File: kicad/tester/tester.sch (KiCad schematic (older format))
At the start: 9 parts, among them J0 ST7735, U1 STM32F103C8Tx, U2 LMV324, Y1 8Mhz

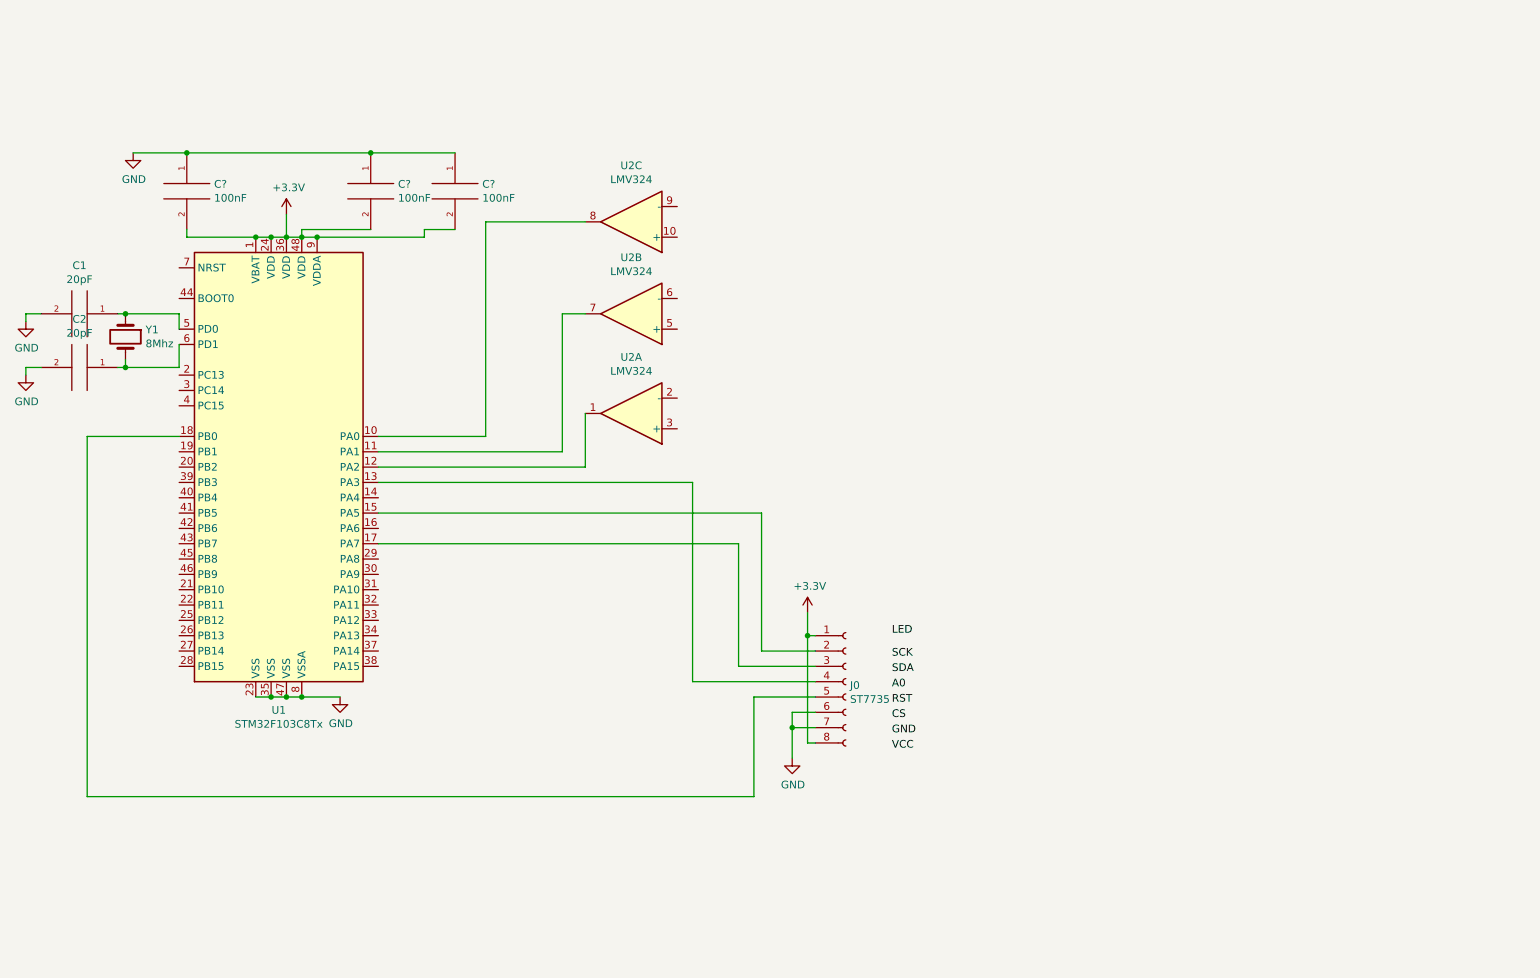
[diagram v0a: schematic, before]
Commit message: kicad : update schematic
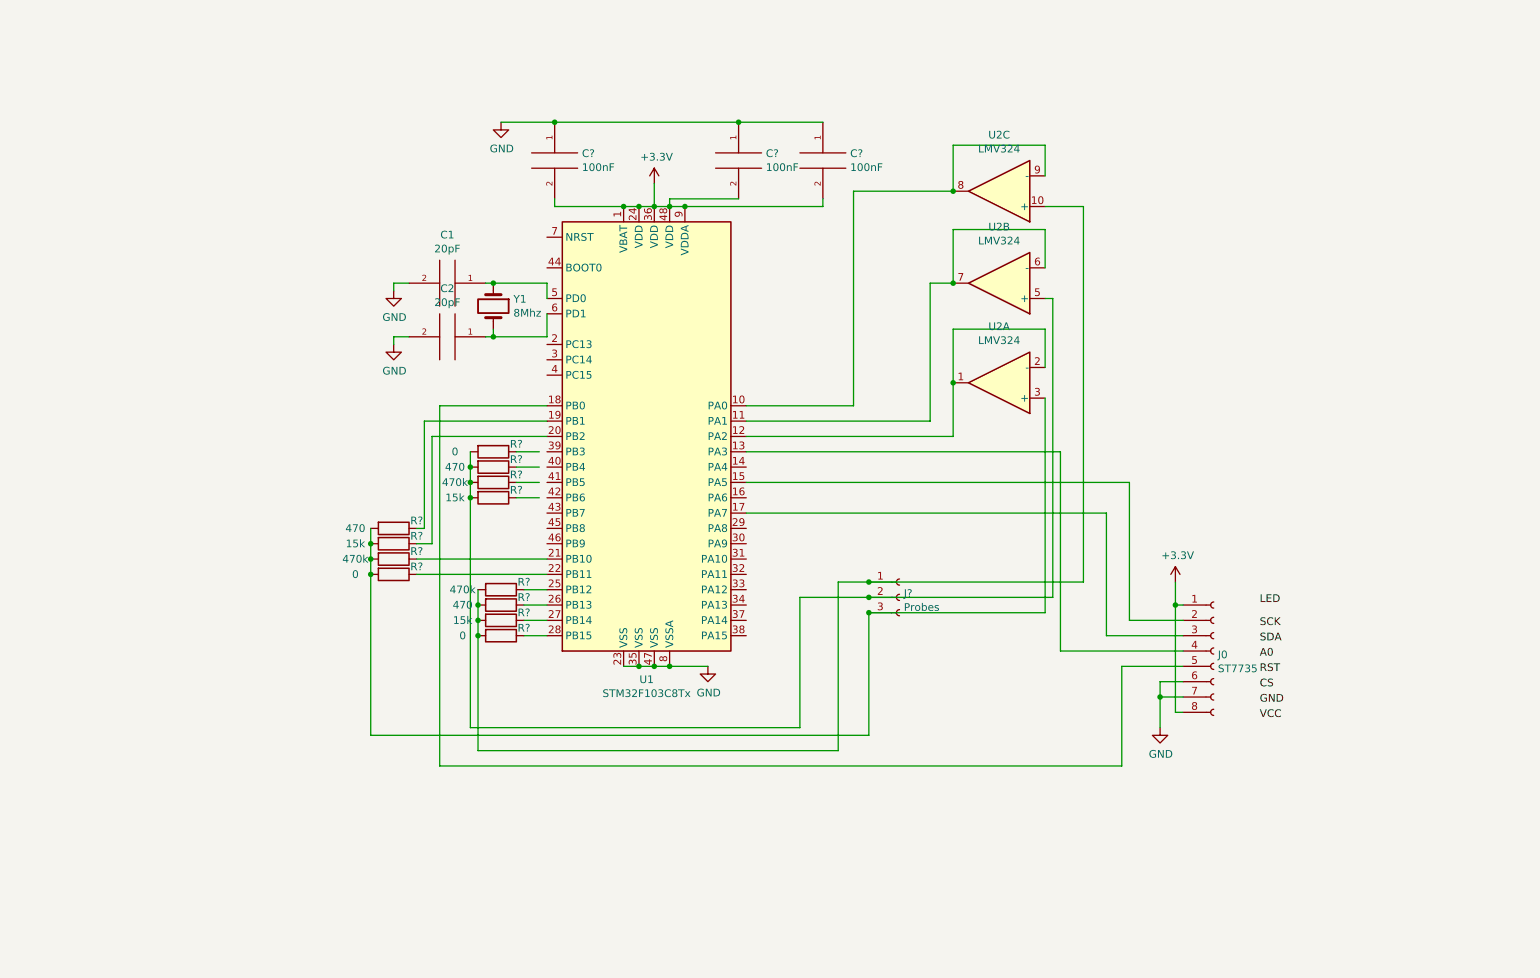
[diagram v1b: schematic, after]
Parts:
- added J?: Probes, symbol Connector:Conn_01x03_Female
- added R? (x3): 470, symbol Device:R
- added R? (x3): 15k, symbol Device:R
- added R? (x3): 0, symbol Device:R
- added R? (x3): 470k, symbol Device:R
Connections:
- wire segments 60 -> 112
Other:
- moved on the sheet: C1, C2, C?, J0, U1, U2A, U2B, U2C, Y1

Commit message: update schematic
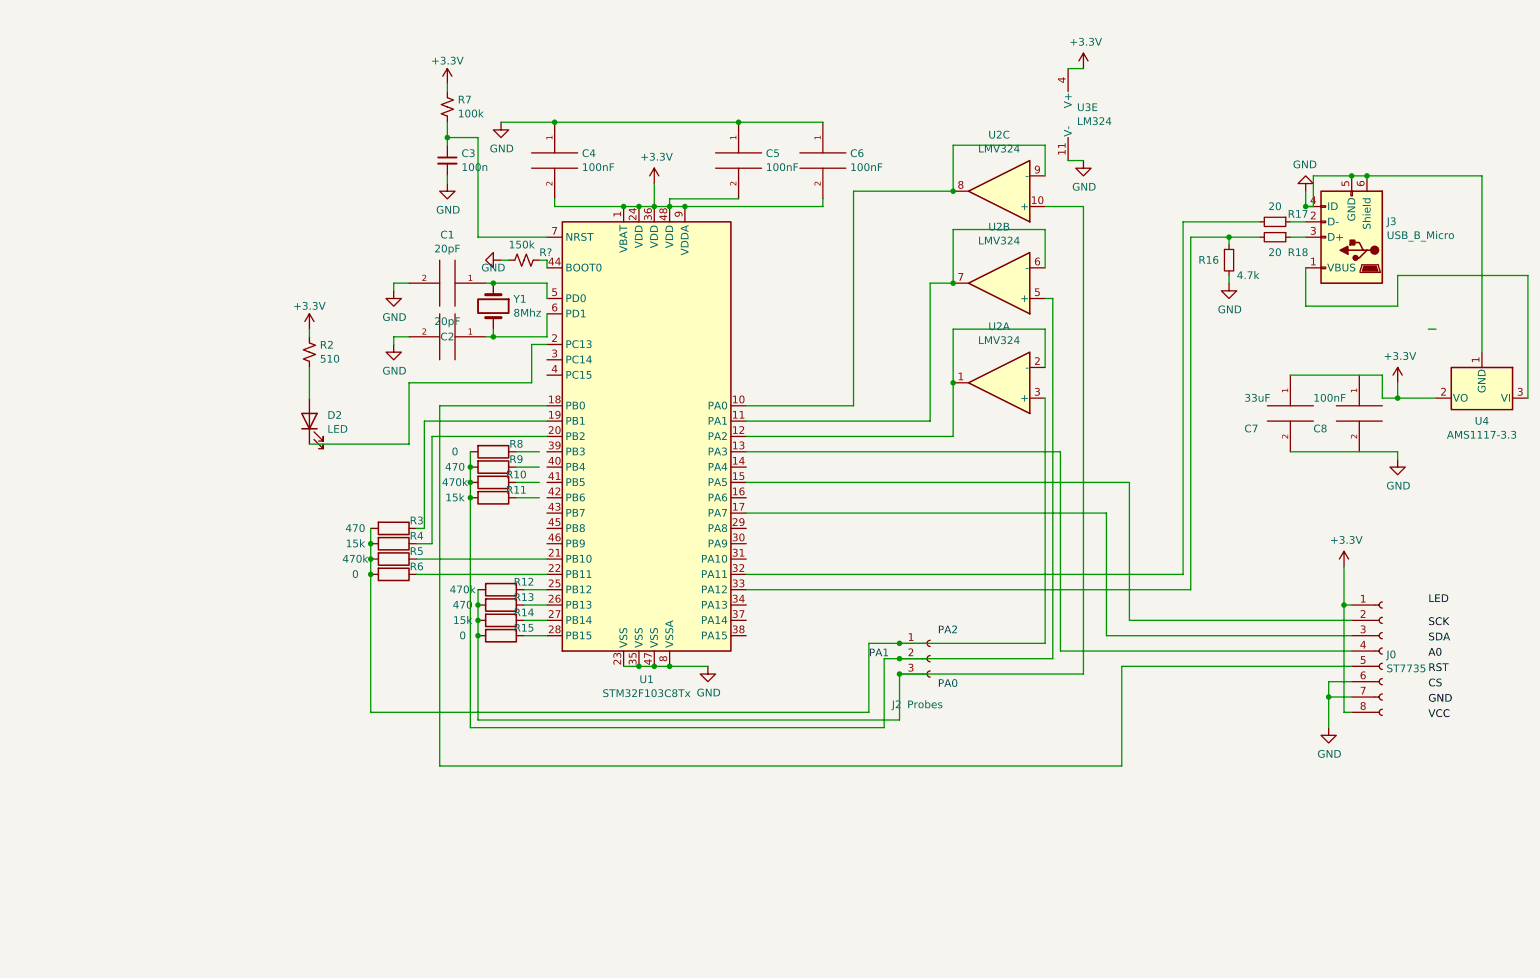
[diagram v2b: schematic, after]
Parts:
- added C3: 100n, symbol Device:C_Small
- added C7: 33uF, symbol pspice:C
- added C8: 100nF, symbol pspice:C
- added D2: LED, symbol Device:LED
- added J3: USB_B_Micro, symbol Connector:USB_B_Micro
- added R16: 4.7k, symbol Device:R_Small
- added R17, R18: 20, symbol Device:R_Small
- added R2: 510, symbol Device:R_Small_US
- added R7: 100k, symbol Device:R_Small_US
- added R?: 150k, symbol Device:R_Small_US
- added U3: LM324, symbol Amplifier_Operational:LM324
- added U4: AMS1117-3.3, Package_TO_SOT_SMD:SOT-223-3_TabPin2, symbol Regulator_Linear:AMS1117-3.3
- gave numbers to parts that had none: 16
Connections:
- wire segments 112 -> 162
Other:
- note added: "PA0\n"
- note added: "PA1"
- note added: "PA2"
- moved on the sheet: J0, J2

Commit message: Print out configuraiton on the splash screen
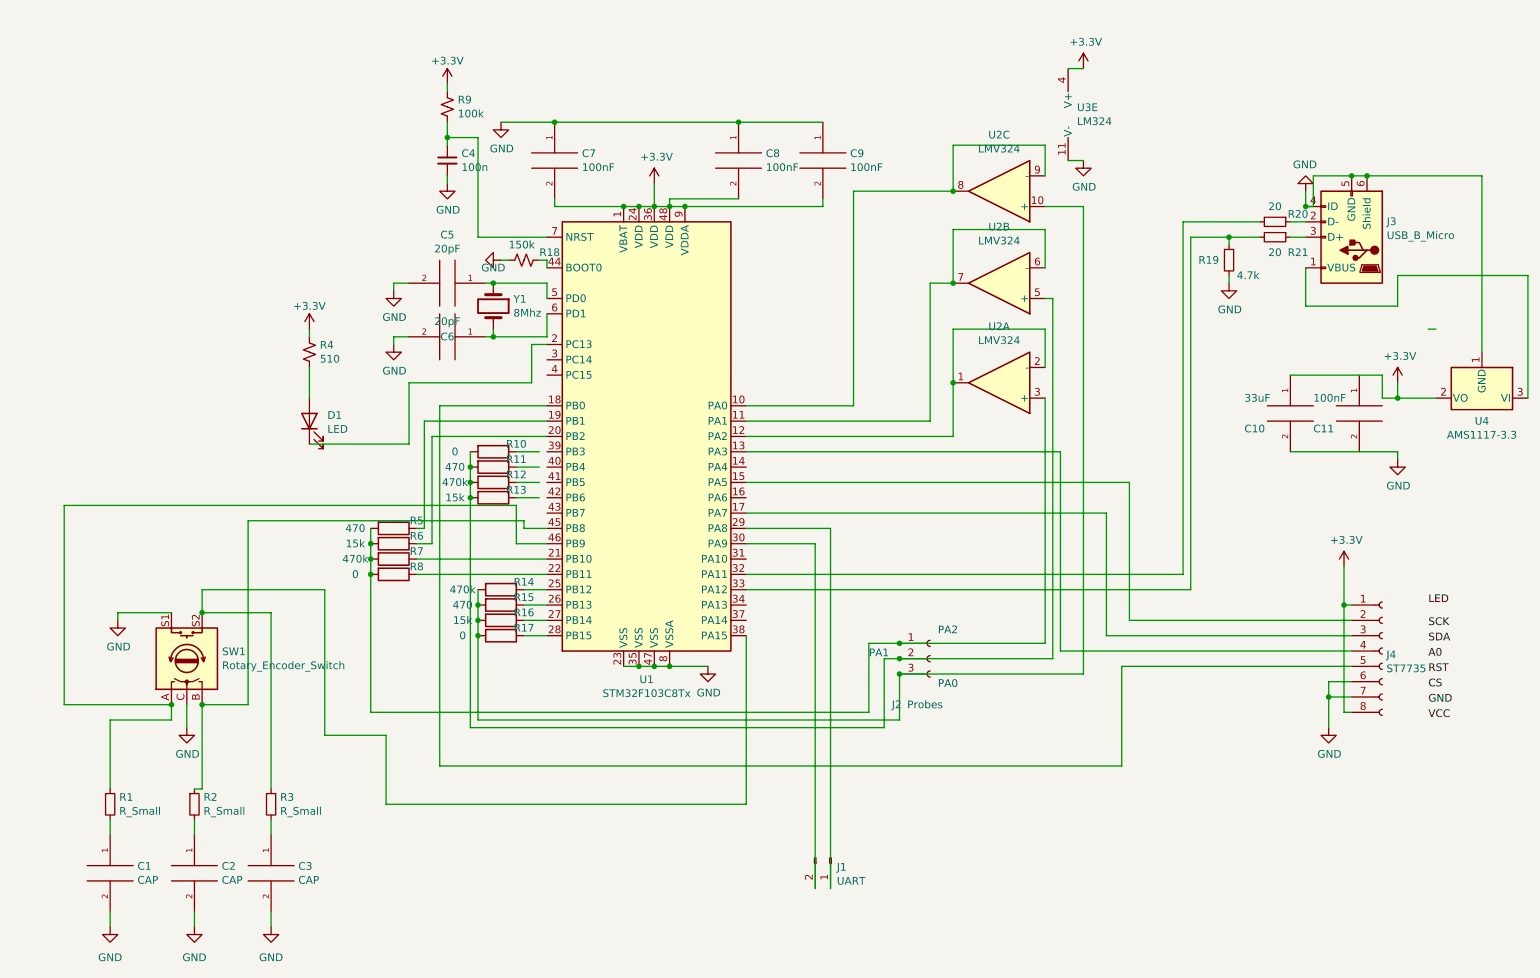
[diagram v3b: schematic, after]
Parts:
- added C1, C2, C3: CAP, symbol pspice:CAP
- added J1: UART, symbol Connector:Conn_01x02_Male
- added R1, R2, R3: R_Small, symbol Device:R_Small
- added SW1: Rotary_Encoder_Switch, symbol Device:Rotary_Encoder_Switch
- J4: renamed from J0; footprint VCC -> (none)
- gave numbers to parts that had none: 1
- renumbered C7 to C10, C8 to C11, C3 to C4, C1 to C5, C2 to C6, C4 to C7, C5 to C8, C6 to C9, D2 to D1, R8 to R10, R9 to R11, R10 to R12, R11 to R13, R12 to R14, R13 to R15, R14 to R16, R15 to R17, R16 to R19, R17 to R20, R18 to R21, R2 to R4, R3 to R5, R4 to R6, R5 to R7, R6 to R8, R7 to R9
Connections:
- wire segments 162 -> 199

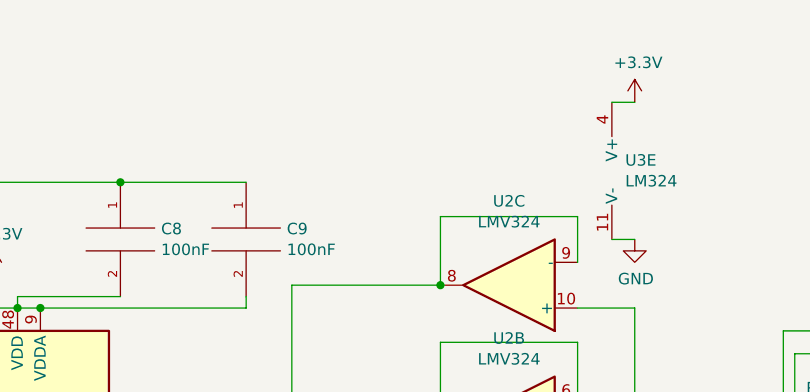
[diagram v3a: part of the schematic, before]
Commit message: begin cleaning up gfx
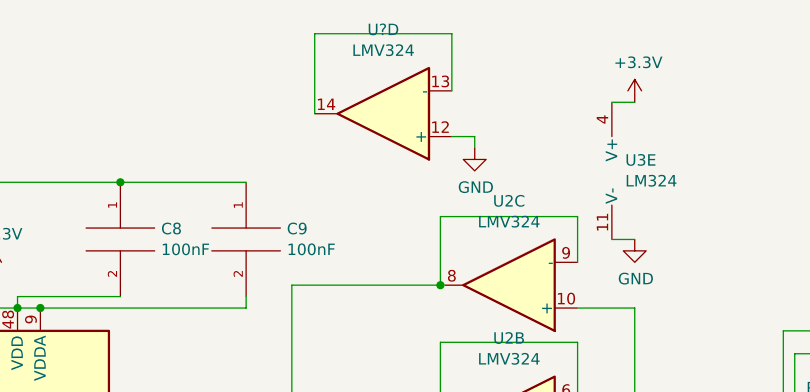
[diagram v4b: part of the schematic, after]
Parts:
- added U?: LMV324, symbol Amplifier_Operational:LMV324
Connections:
- wire segments 199 -> 204
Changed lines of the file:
@@
 Wire Wire Line
 	5900 3850 5900 6200
+$Comp
+L Amplifier_Operational:LMV324 U?
+U 4 1 5E7D1B3F
+P 6450 900
+F 0 "U?" H 6450 533 50  0000 C CNN
+F 1 "LMV324" H 6450 624 50  0000 C CNN
+F 2 "" H 6400 1000 50  0001 C CNN
+F 3 "http://www.ti.com/lit/ds/symlink/lmv324.pdf" H 6500 1100 50  0001 C CNN
+	4    6450 900
+	-1   0    0    1
+$EndComp
+Wire Wire Line
+	6750 800  6750 550
+Wire Wire Line
+	6750 550  6150 550
+Wire Wire Line
+	6150 550  6150 900
+$Comp
+L power:GND #PWR?
+U 1 1 5E7DD9B3
+P 6850 1050
+F 0 "#PWR?" H 6850 800 50  0001 C CNN
+F 1 "GND" H 6855 877 50  0000 C CNN
+F 2 "" H 6850 1050 50  0001 C CNN
+F 3 "" H 6850 1050 50  0001 C CNN
+	1    6850 1050
+	1    0    0    -1
+$EndComp
+Wire Wire Line
+	6750 1000 6850 1000
+Wire Wire Line
+	6850 1000 6850 1050
 $EndSCHEMATC

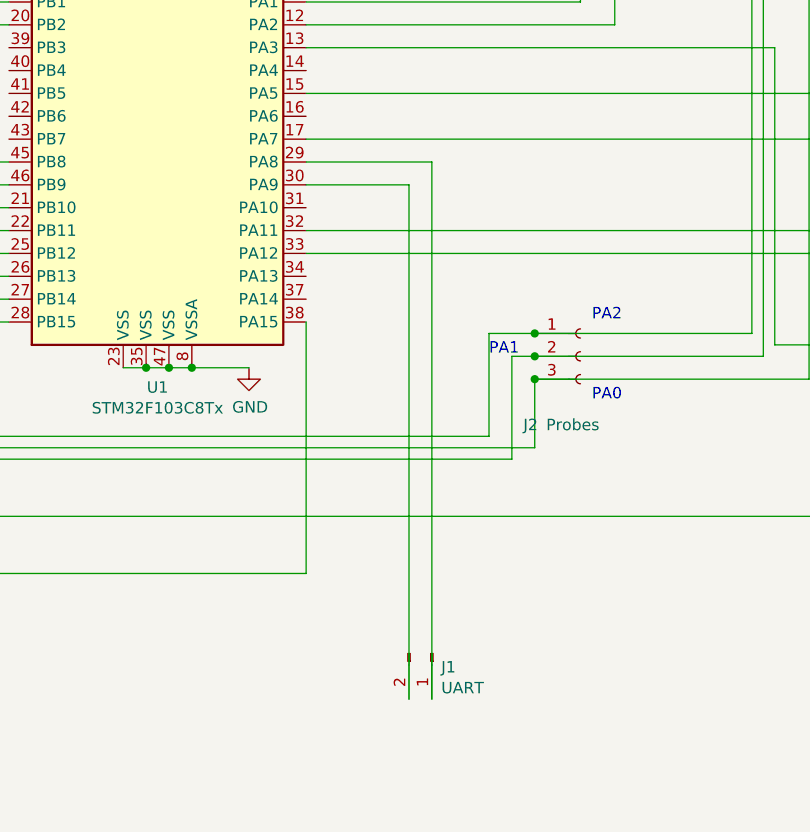
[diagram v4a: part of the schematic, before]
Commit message: update schematic, fix rx/tx uart pin
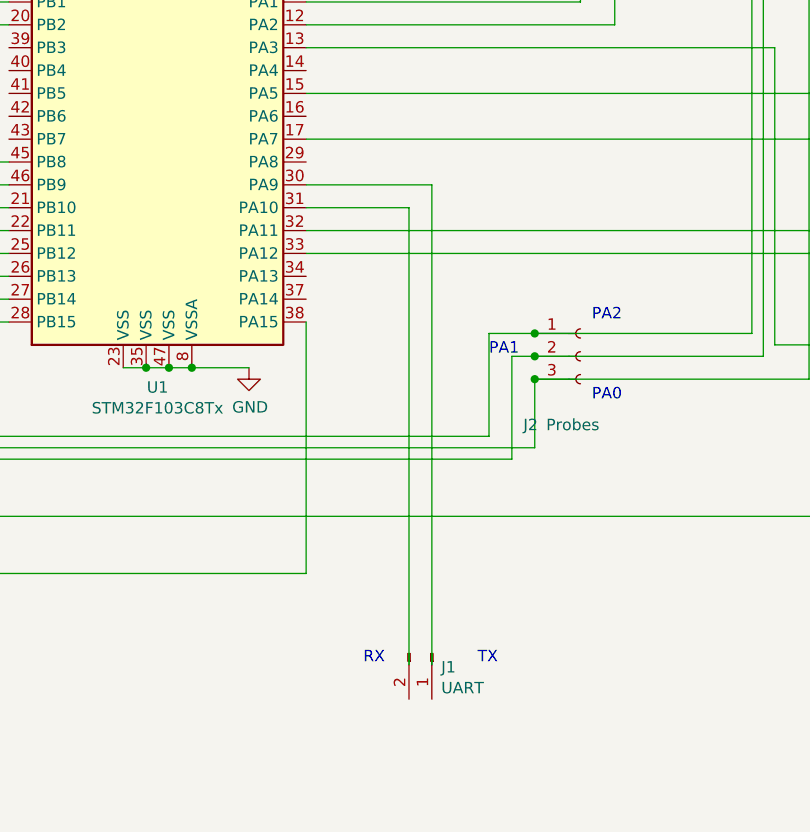
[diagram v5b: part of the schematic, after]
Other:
- note added: "RX"
- note added: "TX"
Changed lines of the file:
@@
 EESchema Schematic File Version 4
-LIBS:tester-cache
-EELAYER 26 0
+EELAYER 30 0
 EELAYER END
 $Descr A4 11693 8268
@@
 	0    1    1    0
 $EndComp
-Wire Wire Line
-	5350 3950 5800 3950
-Wire Wire Line
-	5800 3950 5800 6200
-Wire Wire Line
-	5350 3850 5900 3850
-Wire Wire Line
-	5900 3850 5900 6200
 $Comp
 L Amplifier_Operational:LMV324 U?
@@
 Wire Wire Line
 	6850 1000 6850 1050
+Wire Wire Line
+	5800 6050 5800 4050
+Wire Wire Line
+	5800 4050 5350 4050
+Wire Wire Line
+	5900 6050 5900 3950
+Wire Wire Line
+	5900 3950 5350 3950
+Text Notes 6100 6050 0    50   ~ 0
+TX
+Text Notes 5600 6050 0    50   ~ 0
+RX
 $EndSCHEMATC

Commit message: branch
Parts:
- J3: symbol Connector:USB_B_Micro -> tester-rescue:USB_B_Micro-Connector
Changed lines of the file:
@@
 	2500 2800 2500 3000
 $Comp
-L Connector:USB_B_Micro J3
+L tester-rescue:USB_B_Micro-Connector J3
 U 1 1 5E792D53
 P 9300 1950
